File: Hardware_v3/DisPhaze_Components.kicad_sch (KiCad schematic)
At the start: 83 parts, among them J1 SWD_Header, J2 Eurorack_16_pin_power, J3 PD1_Amt_In, J4 DAC1_Out, J5 PItch_In, J6 DAC2_Out, J7 PD2_Amt_In, J8 VCA_In, J9 USB_B_Micro, SW1 Octave_Switch, SW2 DAC1_RingMod_Switch, SW3 DAC2_Mix_Switch, SW4 SW_Push, U1 TL072, U2 MCP6004, U3 LM1117-3.3, U4 STM32F405RGTx, U5 LM4040DBZ-5, Y1 12MHz

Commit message: Updated panel to incorporate v3 redesign
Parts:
- CTune1, FTune1, PD1Amt1, PD1Type1, PD2Amt1, PD2Type1: footprint Custom_Footprints:Alpha_9mm_Potentiometer -> Custom_Footprints:Alpha_9mm_Potentiometer_Aligned
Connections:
- net Action renamed ACTION
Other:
- note added: "MCU"
- note removed: "To Do: Add Reset button Ground Boot0 Capacitors to VDDA input UART/USB IO?"
- moved on the sheet: C1, C10, C11, C12, C13, C14, C15, C16, C17, C18, C19, C2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

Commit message: Added photocoupler to MIDI Input
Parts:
- added R20, R21: (no value), symbol Device:R_Small
- added U4: (no value), symbol Isolator:LTV-356T
- renumbered C8 to C1, C12 to C11, C13 to C12, C9 to C13, C16 to C14, C14 to C15, C17 to C16, C21 to C17, C22 to C18, C24 to C19, C15 to C2, C18 to C20, C19 to C21, C20 to C22, C11 to C24, C1 to C3, C2 to C4, C3 to C5, C4 to C6, C5 to C7, C6 to C8, C7 to C9, D3 to D1, D1 to D2, D2 to D3, J5 to J1, J4 to J2, J6 to J4, J7 to J5, J1 to J6, J9 to J7, J2 to J9, R9 to R1, R3 to R10, R5 to R12, R18 to R16, R19 to R17, R20 to R18, R21 to R19, R10 to R2, R16 to R25, R17 to R26, R2 to R3, R12 to R4, R4 to R5, R8 to R7, R7 to R8, R1 to R9, TP5 to TP1, TP1 to TP2, TP2 to TP3, TP3 to TP4, TP4 to TP5, U2 to U1, U1 to U2, U4 to U3, U3 to U5, U5 to U6
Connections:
- net +3V3: now also R20.1
- net GND: now also U4.3
- net MIDI_RX: now also R20.2, U4.4; no longer C2.2, R2.1, U1.1, U3.26 (PB0)
- net MIDI_VREF: now reaches J1.R
- net MIDI_VREF: now also R21.2
- net Pitch_In renamed Pitch_MIDI_In
- net Pitch_MIDI_In: now also U4.2
- new net: R21.1, U4.1
- new net V_OCT_CV: C2.2, R2.1, U1.1, U3.26 (PB0)
- no-connect marks 31 -> 30
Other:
- note added: "MIDI Optocoupler"
- moved on the sheet: CTune1, FTune1, J1, PD1Amt1, PD1Type1, PD2Amt1, PD2Type1

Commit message: Replaced optocoupler with transistor pair. Changed bi-colour LED to 3 lead device
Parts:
- removed D1: RG_LED, LED_THT:LED_D3.0mm, symbol Device:LED_Dual_Bidirectional
- removed R20, R21: (no value), symbol Device:R_Small
- removed U4: (no value), symbol Isolator:LTV-356T
- added D1: (no value), symbol Device:LED_Dual_AKA
- added Q1, Q2: (no value), symbol Transistor_BJT:MMBT3904
- added R25, R26, R27, R3: (no value), symbol Device:R_Small
- C1: renamed from C3; value 4.7uF -> (none); footprint Capacitor_SMD:C_0603_1608Metric -> (none)
- C10: renamed from C15; value 18pF -> (none); footprint Capacitor_SMD:C_0603_1608Metric -> (none)
- C11: renamed from C16; value 18pF -> (none); footprint Capacitor_SMD:C_0603_1608Metric -> (none)
- C12: renamed from C2; value 2.2nF -> (none); footprint Capacitor_SMD:C_0603_1608Metric -> (none)
- C13: value 1.5nF -> (none); footprint Capacitor_SMD:C_0603_1608Metric -> (none)
- C14: renamed from C18; value 2.2nF -> (none); footprint Capacitor_SMD:C_0603_1608Metric -> (none)
- C15: renamed from C19; value 1.5nF -> (none); footprint Capacitor_SMD:C_0603_1608Metric -> (none)
- C16: renamed from C1; value 18pF -> (none); footprint Capacitor_SMD:C_0603_1608Metric -> (none)
- C17: renamed from C10; value 10uF -> (none); footprint Capacitor_SMD:C_0603_1608Metric -> (none)
- C18: renamed from C14; value 18pF -> (none); footprint Capacitor_SMD:C_0603_1608Metric -> (none)
- C19: renamed from C17; value 10uF -> (none); footprint Capacitor_SMD:C_0603_1608Metric -> (none)
- C2: renamed from C4; value 100nF -> (none); footprint Capacitor_SMD:C_0603_1608Metric -> (none)
- C20: value 10uF -> (none); footprint Capacitor_SMD:C_0805_2012Metric -> (none)
- C21, C24: value 22uF -> (none); footprint Capacitor_SMD:CP_Elec_4x5.3 -> (none)
- C22: value 47uF -> (none); footprint Capacitor_SMD:CP_Elec_5x5.4 -> (none)
- C23: value 100nF -> (none); footprint Capacitor_SMD:C_0603_1608Metric -> (none)
- C3: renamed from C5; value 100nF -> (none); footprint Capacitor_SMD:C_0603_1608Metric -> (none)
- C4: renamed from C6; value 100nF -> (none); footprint Capacitor_SMD:C_0603_1608Metric -> (none)
- C5: renamed from C7; value 100nF -> (none); footprint Capacitor_SMD:C_0603_1608Metric -> (none)
- C6: renamed from C8; value 1uF -> (none); footprint Capacitor_SMD:C_0603_1608Metric -> (none)
- C7: renamed from C9; value 100nF -> (none); footprint Capacitor_SMD:C_0603_1608Metric -> (none)
- C8: renamed from C11; value 2.2uF -> (none); footprint Capacitor_SMD:C_0603_1608Metric -> (none)
- C9: renamed from C12; value 2.2uF -> (none); footprint Capacitor_SMD:C_0603_1608Metric -> (none)
- CTune1, FTune1, PD1Amt1, PD1Type1, PD2Amt1, PD2Type1: value B10k -> (none); footprint Custom_Footprints:Alpha_9mm_Potentiometer_Aligned -> (none)
- D2, D3: value 1N5819 -> (none); footprint Diode_SMD:D_SOD-123 -> (none)
- J1: renamed from J6; value SWD_Header -> (none); footprint Custom_Footprints:SWD_header -> (none)
- J2: renamed from J7; value USB_B_Micro -> (none); footprint Custom_Footprints:USB_TE_1734517-1 -> (none)
- J3: renamed from J1; value PItch_In -> (none); footprint Custom_Footprints:Thonkiconn_Stereo-PJ366ST -> (none)
- J4: renamed from J3; value PD1_Amt_In -> (none); footprint Custom_Footprints:THONKICONN_hole -> (none)
- J5: value PD2_Amt_In -> (none); footprint Custom_Footprints:THONKICONN_hole -> (none)
- J6: renamed from J8; value VCA_In -> (none); footprint Custom_Footprints:THONKICONN_hole -> (none)
- J7: renamed from J2; value DAC1_Out -> (none); footprint Custom_Footprints:THONKICONN_hole -> (none)
- J8: renamed from J4; value DAC2_Out -> (none); footprint Custom_Footprints:THONKICONN_hole -> (none)
- J9: value Eurorack_16_pin_power -> (none); footprint Custom_Footprints:Eurorack_16_pin_header -> (none)
- L1: value L -> (none); footprint Inductor_SMD:L_0805_2012Metric -> (none)
- R1: renamed from R8; value 100k -> (none); footprint Resistor_SMD:R_0603_1608Metric -> (none)
- R10: renamed from R16; value 68k -> (none); footprint Resistor_SMD:R_0603_1608Metric -> (none)
- R11: renamed from R17; value 47k -> (none); footprint Resistor_SMD:R_0603_1608Metric -> (none)
- R12: renamed from R18; value 100k -> (none); footprint Resistor_SMD:R_0603_1608Metric -> (none)
- R13: renamed from R19; value 68k -> (none); footprint Resistor_SMD:R_0603_1608Metric -> (none)
- R14: renamed from R22; value 47k -> (none); footprint Resistor_SMD:R_0603_1608Metric -> (none)
- R15: renamed from R23; value 47k -> (none); footprint Resistor_SMD:R_0603_1608Metric -> (none)
- R16: renamed from R24; value 100k -> (none); footprint Resistor_SMD:R_0603_1608Metric -> (none)
- R17: renamed from R3; value 68k -> (none); footprint Resistor_SMD:R_0603_1608Metric -> (none)
- R18: renamed from R5; value 6.8k -> (none); footprint Resistor_SMD:R_0603_1608Metric -> (none)
- R19: renamed from R6; value 1k -> (none); footprint Resistor_SMD:R_0603_1608Metric -> (none)
- R2: renamed from R25; value 1k -> (none); footprint Resistor_SMD:R_0603_1608Metric -> (none)
- R20: renamed from R7; value 47k -> (none); footprint Resistor_SMD:R_0603_1608Metric -> (none)
- R21: renamed from R11; value 68k -> (none); footprint Resistor_SMD:R_0603_1608Metric -> (none)
- R22: renamed from R13; value 6.8k -> (none); footprint Resistor_SMD:R_0603_1608Metric -> (none)
- R23: renamed from R14; value 1k -> (none); footprint Resistor_SMD:R_0603_1608Metric -> (none)
- R24: renamed from R15; value 47k -> (none); footprint Resistor_SMD:R_0603_1608Metric -> (none)
- R28: renamed from R26; value 2.2k -> (none); footprint Resistor_SMD:R_0603_1608Metric -> (none)
- R4: renamed from R1; value 91k -> (none); footprint Resistor_SMD:R_0603_1608Metric -> (none)
- R5: renamed from R2; value 56k -> (none); footprint Resistor_SMD:R_0603_1608Metric -> (none)
- R6: renamed from R4; value 100k -> (none); footprint Resistor_SMD:R_0603_1608Metric -> (none)
- R7: renamed from R9; value 82k -> (none); footprint Resistor_SMD:R_0603_1608Metric -> (none)
- R8: renamed from R10; value 47k -> (none); footprint Resistor_SMD:R_0603_1608Metric -> (none)
- R9: renamed from R12; value 100k -> (none); footprint Resistor_SMD:R_0603_1608Metric -> (none)
- RESET1: value SW_Push -> (none); footprint Custom_Footprints:SW_SPST_EVQQ2 -> (none)
- SW1: value Octave_Switch -> (none); footprint Custom_Footprints:SPDTSubMiniature -> (none)
- SW2: value DAC1_RingMod_Switch -> (none); footprint Custom_Footprints:SPDTSubMiniature -> (none)
- SW3: value DAC2_Mix_Switch -> (none); footprint Custom_Footprints:SPDTSubMiniature -> (none)
- SW4: value SW_Push -> (none); footprint Custom_Footprints:SW_PUSH_6mm_aligned -> (none)
- TP1, TP2, TP3, TP4, TP5: value TestPoint -> (none); footprint Custom_Footprints:1.3mm_Test_Point -> (none)
- U1: renamed from U3; value STM32F405RGTx -> (none); footprint Package_QFP:LQFP-64_10x10mm_P0.5mm -> (none)
- U2: value TL072 -> (none); footprint Package_SO:SOIC-8_3.9x4.9mm_P1.27mm -> (none)
- U3: renamed from U1; value MCP6004 -> (none); footprint Package_SO:SOIC-14_3.9x8.7mm_P1.27mm -> (none)
- U4: renamed from U5; value LM1117-3.3 -> (none); footprint Package_TO_SOT_SMD:SOT-223-3_TabPin2 -> (none)
- U7: renamed from U6; value LM4040DBZ-5 -> (none); footprint Package_TO_SOT_SMD:SOT-23 -> (none)
- Y1: value 12MHz -> (none); footprint Crystal:Crystal_SMD_0603-2Pin_6.0x3.5mm -> (none)
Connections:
- net +3V3: now also R25.2, R26.2
- net GND: now also D1.2 (K), Q1.2 (E), Q2.2 (E)
- net LED_GREEN: now also U1.59 (PB7), R3.2; no longer U1.55 (PB3)
- net LED_RED: now also U1.55 (PB3); no longer U1.59 (PB7)
- net MIDI_RX: now also Q2.3 (C), R26.1
- net Pitch_MIDI_In: now also R27.1
- net at R2.1: now also D1.1 (A1)
- net MIDI_VREF: no longer names the net of J3.R
- new net: Q1.3 (C), Q2.1 (B), R25.1
- new net: D1.3 (A2), R3.1
- new net: Q1.1 (B), R27.2
- no-connect marks 30 -> 31
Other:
- note added: "MIDI Level Shifter"
- note removed: "MIDI Optocoupler"
- moved on the sheet: J3, R2

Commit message: Preparation of Gerbers for v3 hardware ordering
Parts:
- C1: value (none) -> 4.7uF; footprint (none) -> Capacitor_SMD:C_0603_1608Metric
- C10, C11, C16, C18: value (none) -> 18pF; footprint (none) -> Capacitor_SMD:C_0603_1608Metric
- C12, C14: value (none) -> 2.2nF; footprint (none) -> Capacitor_SMD:C_0603_1608Metric
- C13, C15: value (none) -> 1.5nF; footprint (none) -> Capacitor_SMD:C_0603_1608Metric
- C17, C19: value (none) -> 10uF; footprint (none) -> Capacitor_SMD:C_0603_1608Metric
- C2, C23, C3, C4, C5, C7: value (none) -> 100nF; footprint (none) -> Capacitor_SMD:C_0603_1608Metric
- C20: value (none) -> 10uF; footprint (none) -> Capacitor_SMD:C_0805_2012Metric
- C21, C24: value (none) -> 22uF; footprint (none) -> Capacitor_SMD:CP_Elec_4x5.3
- C22: value (none) -> 47uF; footprint (none) -> Capacitor_SMD:CP_Elec_5x5.4
- C6: value (none) -> 1uF; footprint (none) -> Capacitor_SMD:C_0603_1608Metric
- C8, C9: value (none) -> 2.2uF; footprint (none) -> Capacitor_SMD:C_0603_1608Metric
- CTune1, FTune1, PD1Amt1, PD1Type1, PD2Amt1, PD2Type1: value (none) -> B10k; footprint (none) -> Custom_Footprints:Alpha_9mm_Potentiometer_Aligned
- D1: value (none) -> LED_Dual_AKA; footprint (none) -> LED_THT:LED_D3.0mm-3
- D2, D3: value (none) -> 1N5819; footprint (none) -> Diode_SMD:D_SOD-123
- J1: value (none) -> SWD_Header; footprint (none) -> Custom_Footprints:SWD_header
- J2: value (none) -> USB_B_Micro; footprint (none) -> Custom_Footprints:USB_TE_1734517-1
- J3: value (none) -> PItch_In; footprint (none) -> Custom_Footprints:Thonkiconn_Stereo-PJ366ST
- J4: value (none) -> PD1_Amt_In; footprint (none) -> Custom_Footprints:THONKICONN_hole
- J5: value (none) -> PD2_Amt_In; footprint (none) -> Custom_Footprints:THONKICONN_hole
- J6: value (none) -> VCA_In; footprint (none) -> Custom_Footprints:THONKICONN_hole
- J7: value (none) -> DAC1_Out; footprint (none) -> Custom_Footprints:THONKICONN_hole
- J8: value (none) -> DAC2_Out; footprint (none) -> Custom_Footprints:THONKICONN_hole
- J9: value (none) -> Eurorack_16_pin_power; footprint (none) -> Custom_Footprints:Eurorack_16_pin_header
- L1: value (none) -> L; footprint (none) -> Inductor_SMD:L_0805_2012Metric
- Q1, Q2: value (none) -> MMBT3904; footprint (none) -> Package_TO_SOT_SMD:SOT-23
- R1, R12, R16, R6, R9: value (none) -> 100k; footprint (none) -> Resistor_SMD:R_0603_1608Metric
- R10, R13, R17, R21: value (none) -> 68k; footprint (none) -> Resistor_SMD:R_0603_1608Metric
- R11, R14, R15, R20, R24, R8: value (none) -> 47k; footprint (none) -> Resistor_SMD:R_0603_1608Metric
- R18, R22: value (none) -> 6.8k; footprint (none) -> Resistor_SMD:R_0603_1608Metric
- R19, R2, R23, R3: value (none) -> 1k; footprint (none) -> Resistor_SMD:R_0603_1608Metric
- R25, R26, R27: value (none) -> 4k7; footprint (none) -> Resistor_SMD:R_0603_1608Metric
- R28: value (none) -> 2.2k; footprint (none) -> Resistor_SMD:R_0603_1608Metric
- R4: value (none) -> 91k; footprint (none) -> Resistor_SMD:R_0603_1608Metric
- R5: value (none) -> 56k; footprint (none) -> Resistor_SMD:R_0603_1608Metric
- R7: value (none) -> 82k; footprint (none) -> Resistor_SMD:R_0603_1608Metric
- RESET1: value (none) -> SW_Push; footprint (none) -> Custom_Footprints:SW_SPST_EVQQ2
- SW1: value (none) -> Octave_Switch; footprint (none) -> Custom_Footprints:SPDTSubMiniature
- SW2: value (none) -> DAC1_RingMod_Switch; footprint (none) -> Custom_Footprints:SPDTSubMiniature
- SW3: value (none) -> DAC2_Mix_Switch; footprint (none) -> Custom_Footprints:SPDTSubMiniature
- SW4: value (none) -> SW_Push; footprint (none) -> Custom_Footprints:SW_PUSH_6mm_aligned
- TP1, TP2, TP3, TP4, TP5: value (none) -> TestPoint; footprint (none) -> Custom_Footprints:1.3mm_Test_Point
- U1: value (none) -> STM32F405RGTx; footprint (none) -> Package_QFP:LQFP-64_10x10mm_P0.5mm
- U2: value (none) -> TL072; footprint (none) -> Package_SO:SOIC-8_3.9x4.9mm_P1.27mm
- U3: value (none) -> MCP6004; footprint (none) -> Package_SO:SOIC-14_3.9x8.7mm_P1.27mm
- U4: value (none) -> LM1117-3.3; footprint (none) -> Package_TO_SOT_SMD:SOT-223-3_TabPin2
- U7: value (none) -> LM4040DBZ-5; footprint (none) -> Package_TO_SOT_SMD:SOT-23
- Y1: value (none) -> 12MHz; footprint (none) -> Crystal:Crystal_SMD_0603-2Pin_6.0x3.5mm
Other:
- note added: "Pitch Input also used as MIDI in via stereo jack. NB Not isolated as shared ground"
- note removed: "The Pitch Input also be used as a MIDI in. NB Jack must be stereo"
- moved on the sheet: C1, C10, C11, C12, C13, C14, C15, C16, C17, C18, C19, C2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

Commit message: Started implementing v3 Polyphonic changes
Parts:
- C10, C11: value 18pF -> 30pF
- C16, C18: value 18pF -> (none)
- Y1: value 12MHz -> 12MHz_18pF
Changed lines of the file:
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@@
   (symbol (lib_id "Device:Crystal_Small") (at 45.72 80.01 90) (unit 1)
     (in_bom yes) (on_board yes)
-    (property "Reference" "Y1" (id 0) (at 39.37 78.74 90)
+    (property "Reference" "Y1" (id 0) (at 40.64 81.28 90)
       (effects (font (size 1.27 1.27)) (justify right))
     )
-    (property "Value" "12MHz" (id 1) (at 36.83 81.28 90)
+    (property "Value" "12MHz_18pF" (id 1) (at 35.56 85.09 90)
       (effects (font (size 1.27 1.27)) (justify right))
     )
@@
       (effects (font (size 1.27 1.27)) (justify left))
     )
-    (property "Value" "18pF" (id 1) (at 25.4 77.47 90)
+    (property "Value" "30pF" (id 1) (at 25.4 77.47 90)
       (effects (font (size 1.27 1.27)) (justify left))
     )
@@
       (effects (font (size 1.27 1.27)) (justify left))
     )
-    (property "Value" "18pF" (id 1) (at 25.4 85.09 90)
+    (property "Value" "30pF" (id 1) (at 25.4 85.09 90)
       (effects (font (size 1.27 1.27)) (justify left))
     )
@@
     (in_bom yes) (on_board yes)
     (property "Reference" "C18" (id 0) (at 245.11 67.2592 90))
-    (property "Value" "18pF" (id 1) (at 245.11 69.5706 90))
+    (property "Value" "" (id 1) (at 245.11 69.5706 90))
     (property "Footprint" "Capacitor_SMD:C_0603_1608Metric" (id 2) (at 245.11 73.66 0)
       (effects (font (size 1.27 1.27)) hide)
@@
     (in_bom yes) (on_board yes)
     (property "Reference" "C16" (id 0) (at 245.11 18.9992 90))
-    (property "Value" "18pF" (id 1) (at 245.11 21.3106 90))
+    (property "Value" "" (id 1) (at 245.11 21.3106 90))
     (property "Footprint" "Capacitor_SMD:C_0603_1608Metric" (id 2) (at 245.11 25.4 0)
       (effects (font (size 1.27 1.27)) hide)
@@
     )
     (path "/00000000-0000-0000-0000-00005c166f76"
-      (reference "C10") (unit 1) (value "18pF") (footprint "Capacitor_SMD:C_0603_1608Metric")
+      (reference "C10") (unit 1) (value "30pF") (footprint "Capacitor_SMD:C_0603_1608Metric")
     )
     (path "/00000000-0000-0000-0000-00005c166fcd"
-      (reference "C11") (unit 1) (value "18pF") (footprint "Capacitor_SMD:C_0603_1608Metric")
+      (reference "C11") (unit 1) (value "30pF") (footprint "Capacitor_SMD:C_0603_1608Metric")
     )
     (path "/00000000-0000-0000-0000-00005c76cac1"
@@
     )
     (path "/00000000-0000-0000-0000-00005c954fe2"
-      (reference "C16") (unit 1) (value "18pF") (footprint "Capacitor_SMD:C_0603_1608Metric")
+      (reference "C16") (unit 1) (value "22pF") (footprint "Capacitor_SMD:C_0603_1608Metric")
     )
     (path "/00000000-0000-0000-0000-00005c90a131"
@@
     )
     (path "/00000000-0000-0000-0000-00005c9448f4"
-      (reference "C18") (unit 1) (value "18pF") (footprint "Capacitor_SMD:C_0603_1608Metric")
+      (reference "C18") (unit 1) (value "22pF") (footprint "Capacitor_SMD:C_0603_1608Metric")
     )
     (path "/00000000-0000-0000-0000-00005c8247b4"
@@
     )
     (path "/00000000-0000-0000-0000-00005c166a7f"
-      (reference "Y1") (unit 1) (value "12MHz") (footprint "Crystal:Crystal_SMD_0603-2Pin_6.0x3.5mm")
+      (reference "Y1") (unit 1) (value "12MHz_18pF") (footprint "Crystal:Crystal_SMD_0603-2Pin_6.0x3.5mm")
     )
   )

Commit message: Serial MIDI basically working; started adding errata to schematic
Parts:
- C16, C18: value (none) -> 22pF
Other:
- note added: "R4 91k > 82k R5 56k > 47k"
- note added: "R7 82k > 75k R8 47k > 51k"
- note added: "v3 Errata - CV Incorrectly normalled to V/Oct - Change Eurorack connector to 10 pin? - Add UART header"
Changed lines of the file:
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@@
     (effects (font (size 2.54 2.54) (thickness 0.508) bold) (justify left bottom))
+  )
+  (text "v3 Errata\n- CV Incorrectly normalled to V/Oct\n- Change Eurorack connector to 10 pin?\n- Add UART header"
+    (at 309.88 257.81 0)
+    (effects (font (size 1.27 1.27)) (justify left bottom))
   )
   (text "Output Amplifiers" (at 207.01 125.73 0)
@@
     (effects (font (size 2.54 2.54) (thickness 0.508) bold) (justify left bottom))
   )
+  (text "R7 82k > 75k\nR8 47k > 51k" (at 181.61 83.82 0)
+    (effects (font (size 1.27 1.27)) (justify left bottom))
+  )
   (text "Power Sections" (at 16.51 273.05 0)
     (effects (font (size 2.54 2.54) (thickness 0.508) bold) (justify left bottom))
@@
   (text "Switches" (at 207.01 218.44 0)
     (effects (font (size 2.54 2.54) (thickness 0.508) bold) (justify left bottom))
+  )
+  (text "R4 91k > 82k\nR5 56k > 47k" (at 177.8 38.1 0)
+    (effects (font (size 1.27 1.27)) (justify left bottom))
   )
   (text "MIDI Level Shifter" (at 306.07 218.44 0)
@@
     (in_bom yes) (on_board yes)
     (property "Reference" "C18" (id 0) (at 245.11 67.2592 90))
-    (property "Value" "" (id 1) (at 245.11 69.5706 90))
+    (property "Value" "22pF" (id 1) (at 245.11 69.5706 90))
     (property "Footprint" "Capacitor_SMD:C_0603_1608Metric" (id 2) (at 245.11 73.66 0)
       (effects (font (size 1.27 1.27)) hide)
@@
     (in_bom yes) (on_board yes)
     (property "Reference" "C16" (id 0) (at 245.11 18.9992 90))
-    (property "Value" "" (id 1) (at 245.11 21.3106 90))
+    (property "Value" "22pF" (id 1) (at 245.11 21.3106 90))
     (property "Footprint" "Capacitor_SMD:C_0603_1608Metric" (id 2) (at 245.11 25.4 0)
       (effects (font (size 1.27 1.27)) hide)

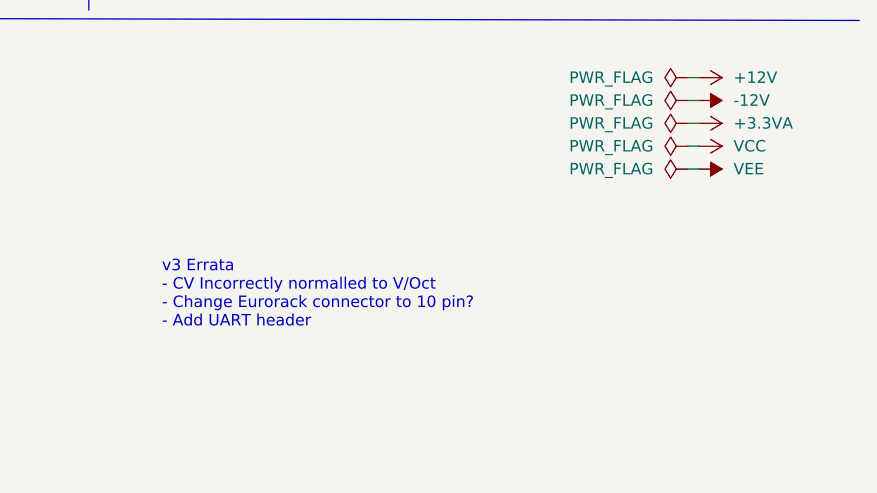
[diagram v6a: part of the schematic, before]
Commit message: Started implementing envelope detection
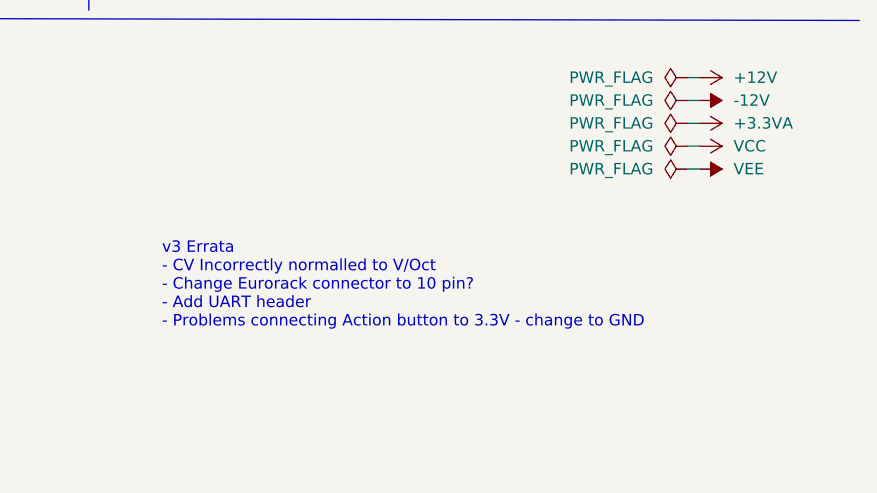
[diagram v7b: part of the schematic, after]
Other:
- note added: "v3 Errata - CV Incorrectly normalled to V/Oct - Change Eurorack connector to 10 pin? - Add UART header - Problems connecting Action button to 3.3V - change to GND"
- note removed: "v3 Errata - CV Incorrectly normalled to V/Oct - Change Eurorack connector to 10 pin? - Add UART header"
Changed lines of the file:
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@@
     (effects (font (size 2.54 2.54) (thickness 0.508) bold) (justify left bottom))
   )
-  (text "v3 Errata\n- CV Incorrectly normalled to V/Oct\n- Change Eurorack connector to 10 pin?\n- Add UART header"
+  (text "v3 Errata\n- CV Incorrectly normalled to V/Oct\n- Change Eurorack connector to 10 pin?\n- Add UART header\n- Problems connecting Action button to 3.3V - change to GND"
     (at 309.88 257.81 0)
     (effects (font (size 1.27 1.27)) (justify left bottom))
